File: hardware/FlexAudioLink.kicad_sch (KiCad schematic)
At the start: 0 parts

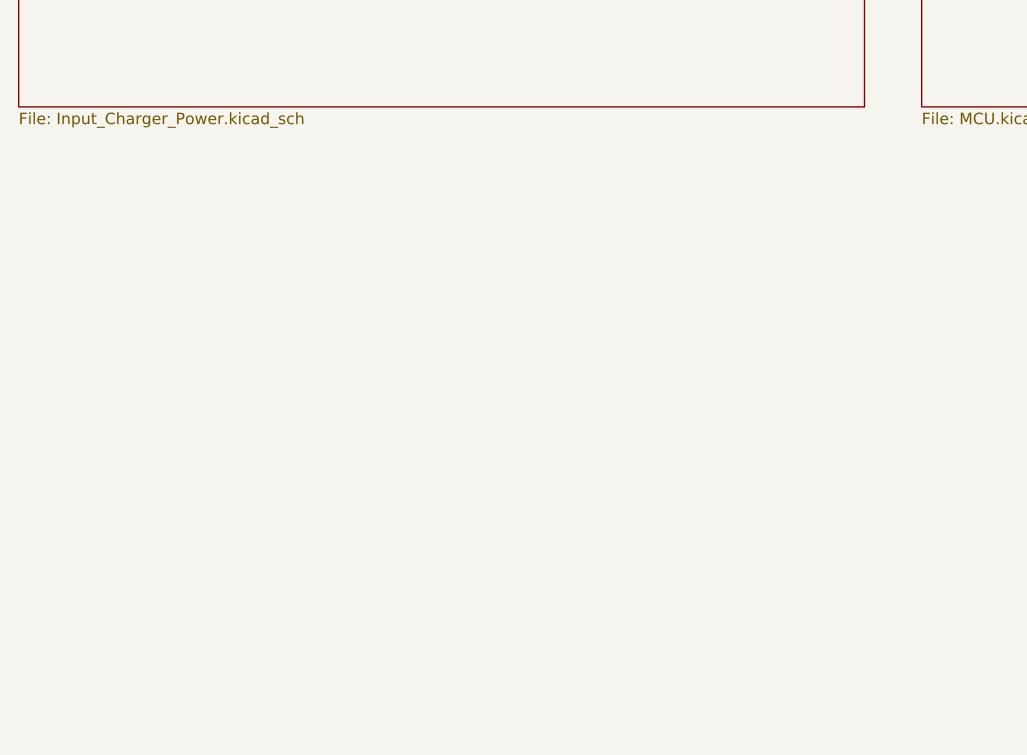
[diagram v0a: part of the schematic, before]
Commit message: Update schematic; Add NAU88L21 schematic symbol;
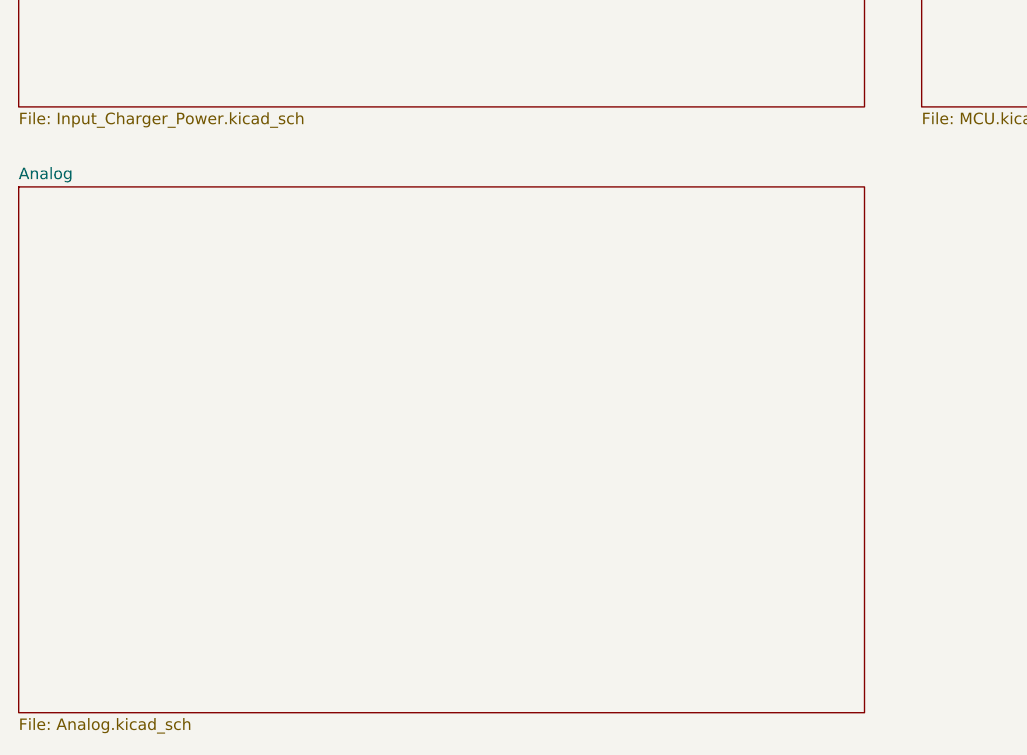
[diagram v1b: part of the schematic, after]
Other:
- added sheet Analog (Analog.kicad_sch)
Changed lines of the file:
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@@
 (kicad_sch
-	(version 20250114)
+	(version 20260306)
 	(generator "eeschema")
-	(generator_version "9.0")
+	(generator_version "10.0")
 	(paper "A4")
+	(sheet
+		(at 25.4 90.17)
+		(size 93.98 58.42)
+		(exclude_from_sim no)
+		(in_bom yes)
+		(on_board yes)
+		(dnp no)
+		(fields_autoplaced yes)
+		(stroke
+			(width 0.1524)
+			(type solid)
+		)
+		(fill
+			(color 0 0 0 0)
+		)
+		(property "Sheetname" "Analog"
+			(at 25.4 89.4584 0)
+			(show_name no)
+			(do_not_autoplace no)
+			(effects
+				(font
+					(size 1.27 1.27)
+				)
+				(justify left bottom)
+			)
+		)
+		(property "Sheetfile" "Analog.kicad_sch"
+			(at 25.4 149.1746 0)
+			(show_name no)
+			(do_not_autoplace no)
+			(effects
+				(font
+					(size 1.27 1.27)
+				)
+				(justify left top)
+			)
+		)
+		(instances
+			(project "FlexAudioLink"
+				(path "/83ca152a-d93c-4f75-91ae-8c2c15978816"
+					(page "4")
+				)
+			)
+		)
+	)
 	(sheet
 		(at 125.73 22.86)
@@
 		)
 		(fill
-			(color 0 0 0 0.0000)
+			(color 0 0 0 0)
 		)
 		(property "Sheetname" "MCU"
 			(at 125.73 22.1484 0)
+			(show_name no)
+			(do_not_autoplace no)
 			(effects
 				(font
@@
 		(property "Sheetfile" "MCU.kicad_sch"
 			(at 125.73 81.8646 0)
+			(show_name no)
+			(do_not_autoplace no)
 			(effects
 				(font
@@
 		)
 		(fill
-			(color 0 0 0 0.0000)
+			(color 0 0 0 0)
 		)
 		(property "Sheetname" "INPUT, CHARGER & POWER"
 			(at 25.4 22.1484 0)
+			(show_name no)
+			(do_not_autoplace no)
 			(effects
 				(font
@@
 		(property "Sheetfile" "Input_Charger_Power.kicad_sch"
 			(at 25.4 81.8646 0)
+			(show_name no)
+			(do_not_autoplace no)
 			(effects
 				(font
